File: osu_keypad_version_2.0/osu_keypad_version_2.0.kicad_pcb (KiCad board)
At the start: 2 copper layers, 99.2 x 49.7 mm, 24 parts, among them SW1 SW_Push, U1 ATmega32U4-A, Y1 16Mhz

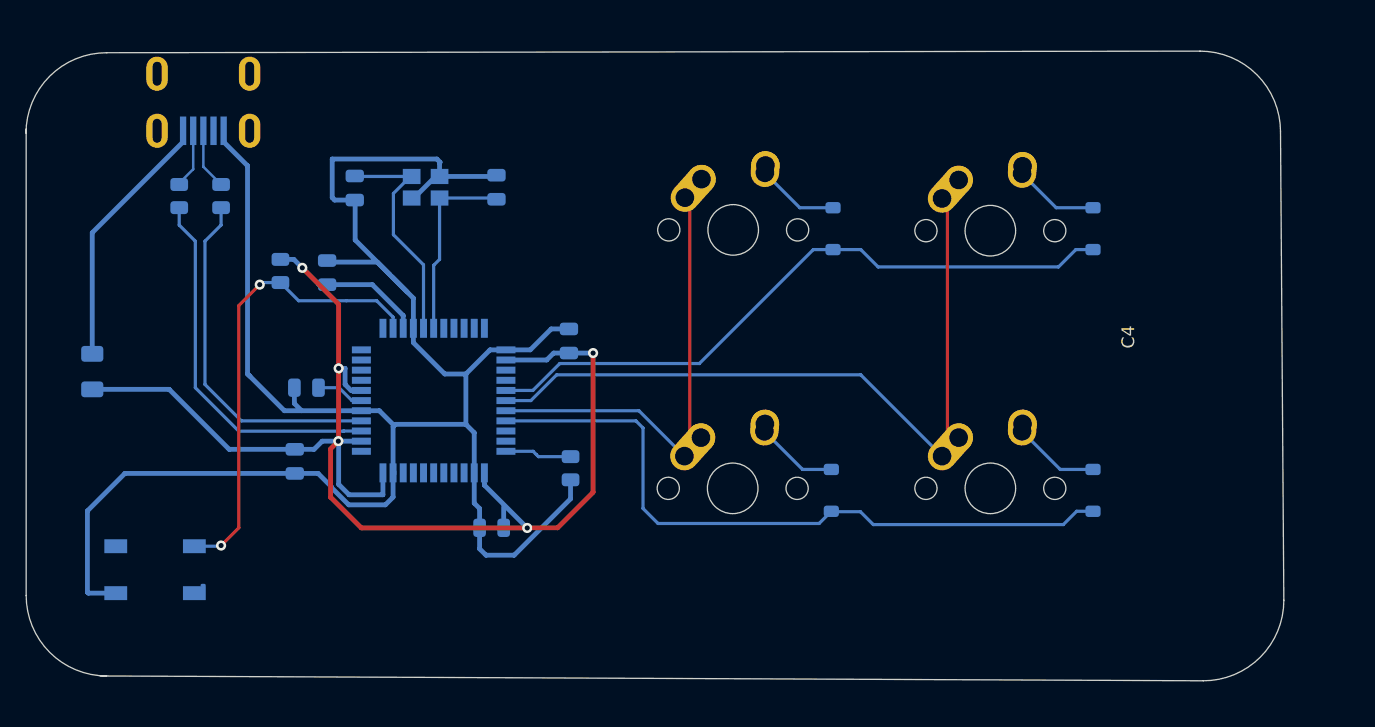
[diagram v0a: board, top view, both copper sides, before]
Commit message: added safe zone
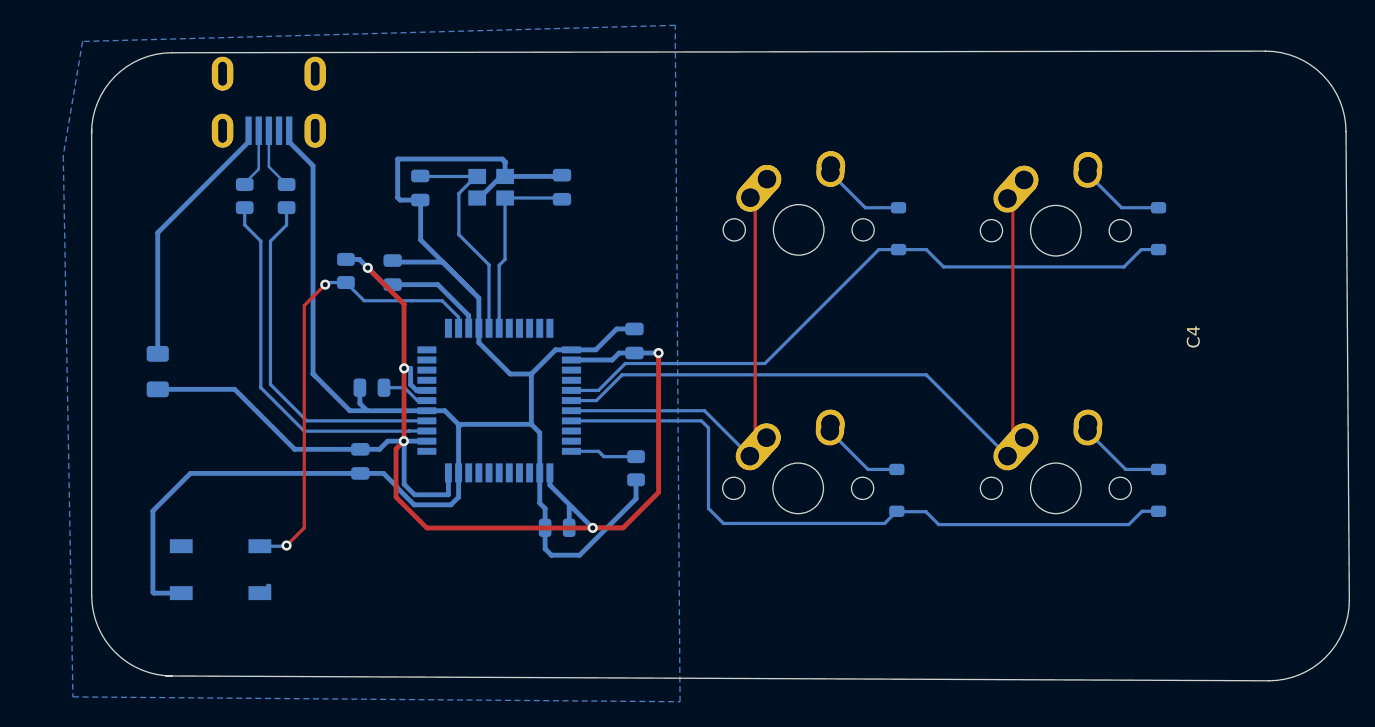
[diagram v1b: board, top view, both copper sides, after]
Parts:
- moved D2 5.17 mm to (156.2, 85.4)
- moved D4 5.17 mm to (156.2, 106.0)
- moved MX2 5.17 mm to (148.1, 85.5)
- moved MX4 5.17 mm to (148.1, 105.9)
- moved C4 5.17 mm to (114.9, 94.2)
- moved F1 5.17 mm to (77.3, 96.6)
- moved MX3 5.17 mm to (127.8, 105.9)
- moved R4 5.17 mm to (92.1, 88.7)
- moved C1 5.17 mm to (94.2, 97.9)
- moved C2 5.17 mm to (108.8, 109.0)
- moved C3 5.17 mm to (95.8, 88.8)
- moved C5 5.17 mm to (93.3, 103.7)
- moved C6 5.17 mm to (109.2, 82.1)
- moved C7 5.17 mm to (98.0, 82.2)
- moved D1 5.17 mm to (135.7, 85.4)
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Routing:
- added copper zone on B.Cu, net GND
